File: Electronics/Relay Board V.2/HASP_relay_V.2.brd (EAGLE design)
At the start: 66.7 x 47.2 mm, 23 parts

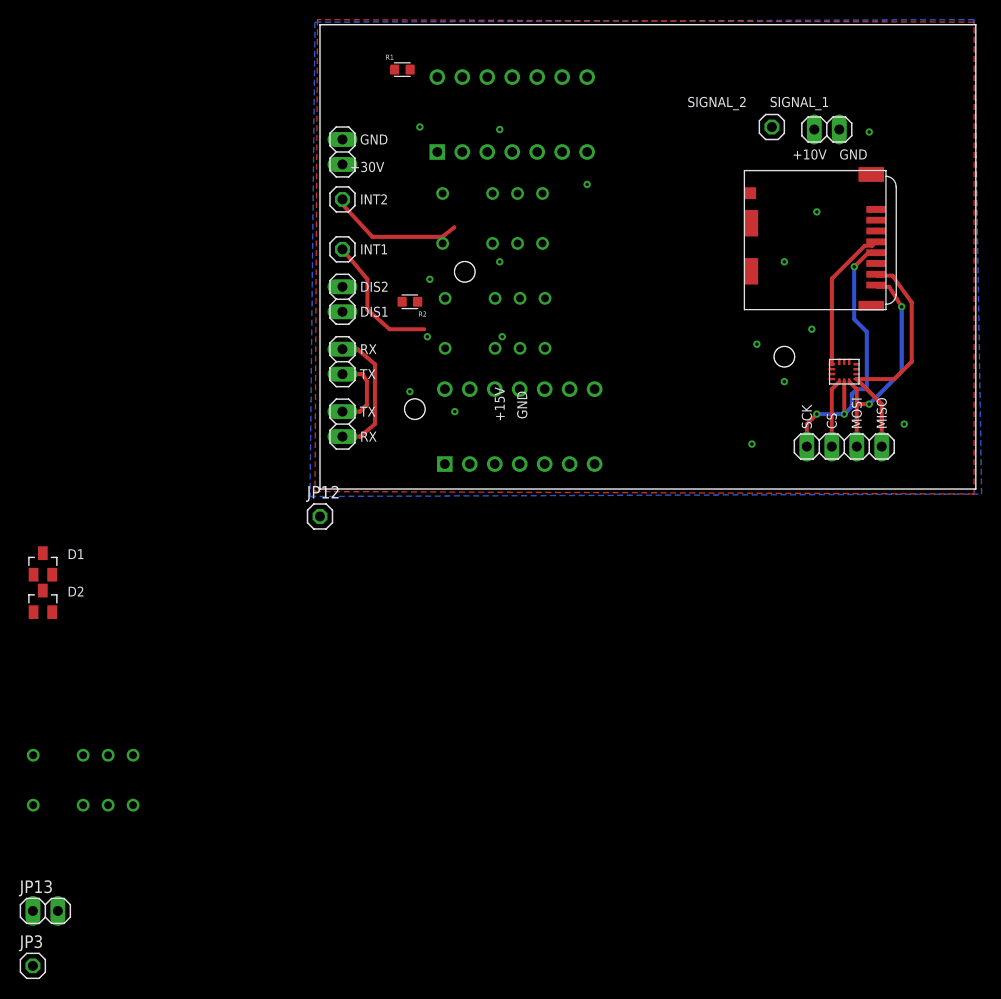
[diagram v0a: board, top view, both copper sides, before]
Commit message: got rid of unnecessary things on relay board, fixed the SD card routing, set up rough pass of board size
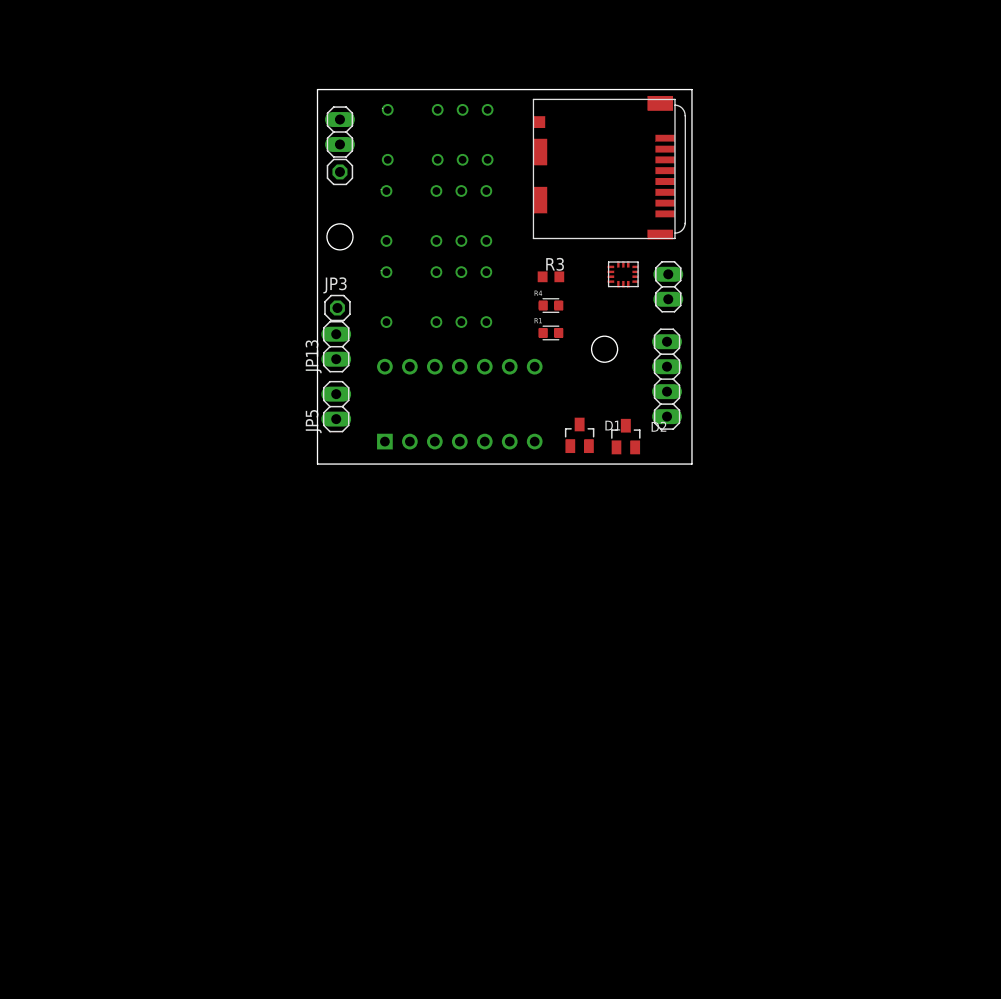
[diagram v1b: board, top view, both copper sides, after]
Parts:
- removed JP12, JP8, JP9: (no value), pinhead:1X01
- removed JP4, JP7: (no value), pinhead:1X02
- removed R2: 47k, CRGS0603J1K5:RESC1608X50N
- removed U$6: CD4093BE, NAND Gates:CD4093BE
- added R3: 1M, resistor:R0603
- added R4: 47k, CRGS0603J1K5:RESC1608X50N
- moved JP3 73.8 mm to (2.03, 15.9)
- moved JP13 64.6 mm to (1.91, 11.9), turned to 90 degrees
- moved D2 61.6 mm to (31.4, 2.79)
- moved U$8 60.9 mm to (5.97, 13.3)
- moved D1 56.2 mm to (26.7, 2.92)
- moved JP10 44.2 mm to (2.29, 29.7)
- moved R1 30.8 mm to (23.7, 13.3)
- moved U$1 24.6 mm to (31.1, 19.3)
- moved JP2 22.7 mm to (35.7, 18.0), turned to 270 degrees
- moved U$4 22.7 mm to (22.0, 33.1)
- moved U$2 20.0 mm to (6.10, 29.8)
- moved JP6 19.3 mm to (35.6, 8.64), turned to 270 degrees
- moved U$5 6.51 mm to (14.5, 6.10)
- moved U$3 5.72 mm to (5.97, 21.6)
- moved JP5 4.62 mm to (1.91, 5.84)
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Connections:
- removed net DIS1: JP4.1
- removed net DIS2: JP4.2
- removed net N$6: U$2.5
- removed net RX: JP5.2, JP7.2
- removed net TX: JP5.1, JP7.1
- new net N$5: U$4.VSS
- net +3V3: now also R3.1, R4.1; no longer R2.2, U$6.P$14
- net COIL2: now also U$5.P$10; no longer U$6.P$3
- net CS: now also R3.2, U$4.CD
- net GND: now also U$4.CD1; no longer U$4.VSS, U$6.P$7
- net INT1: now also JP5.1; no longer JP8.1
- net INT2: now also JP5.2, R4.2, U$5.P$8, U$5.P$9; no longer JP9.1, R2.1, U$6.P$1, U$6.P$2
- net MOSI: now also U$4.CMD; no longer U$4.DAT1
- net OUT1: now also U$2.5
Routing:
- net SCK: track 29.7 -> 0.00 mm, vias 3 -> 0
- net MISO: track 25.4 -> 0.00 mm
- net MOSI: track 23.7 -> 0.00 mm, vias 2 -> 0
- net +3V3: track 14.8 -> 0.00 mm
- net RX: track 13.7 -> 0.00 mm
- net INT2: track 13.7 -> 0.00 mm
- net INT1: track 13.6 -> 0.00 mm
- net TX: track 8.05 -> 0.00 mm
- net CS: track 6.93 -> 0.00 mm
- net GND: track 1.39 -> 0.00 mm, vias 16 -> 0
- removed copper zone on layer 1, net GND
- removed copper zone on layer 16, net GND
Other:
- board size 66.7 x 47.2 mm -> 38.1 x 38.1 mm
- board text removed: "+10V"
- board text removed: "+15V"
- board text removed: "+30V"
- board text removed: "7.2018"
- board text removed: "CS"
- board text removed: "DIS1"
- board text removed: "DIS2"
- board text removed: "GND"
- board text removed: "HASP Relay Board"
- board text removed: "INT1"
- board text removed: "INT2"
- board text removed: "MISO"
- board text removed: "MOSI"
- board text removed: "RX"
- board text removed: "SCK"
- board text removed: "SIGNAL_1"
- board text removed: "SIGNAL_2"
- board text removed: "TX"
- board text removed: "V. 2"

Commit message: Add files via upload
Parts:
- moved D1 24.6 mm to (8.89, 19.9), turned to 180 degrees
- moved D2 21.4 mm to (18.7, 20.1)
- moved U$8 2.79 mm to (5.97, 10.5)
- moved U$1 1.27 mm to (29.8, 19.3)
- moved U$3 0.76 mm to (5.97, 22.4)
- moved U$5 0.76 mm to (14.5, 5.33)
- moved R3 0.51 mm to (23.7, 19.6)
- moved U$2 0.25 mm to (6.10, 30.1)
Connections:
- removed net VDDIO: U$1.5
- net +3V3: now also U$1.5; no longer R1.2, R4.1, U$2.4, U$5.P$14
- net +5V: now also R1.2, R4.1, U$2.4, U$5.P$14
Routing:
- net +5V: track 0.00 -> 65.3 mm, vias 0 -> 1
- net MOSI: track 0.00 -> 48.3 mm, vias 0 -> 2
- net CS: track 0.00 -> 43.5 mm, vias 0 -> 3
- net SCK: track 0.00 -> 39.7 mm, vias 0 -> 2
- net COIL1: track 0.00 -> 39.1 mm, vias 0 -> 2
- net +3V3: track 0.00 -> 38.4 mm, vias 0 -> 2
- net INT2: track 0.00 -> 34.4 mm
- net DASIN: track 0.00 -> 29.3 mm
- net COIL2: track 0.00 -> 25.3 mm
- net DASOUT: track 0.00 -> 24.0 mm
- net OUT1: track 0.00 -> 20.4 mm
- net MISO: track 0.00 -> 19.6 mm, vias 0 -> 2
- net N$3: track 0.00 -> 14.4 mm
- net INT1: track 0.00 -> 11.0 mm
- net GND: track 0.00 -> 10.5 mm, vias 0 -> 2
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- added copper zone on layer 1, net GND
- added copper zone on layer 16, net GND
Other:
- board text added: "3V3"
- board text added: "5V"
- board text added: "7.2018"
- board text added: "ARDIN"
- board text added: "CS"
- board text added: "DASIN"
- board text added: "DASOUT"
- board text added: "GND"
- board text added: "HASP Relay Board"
- board text added: "INT1"
- board text added: "INT2"
- board text added: "MISO"
- board text added: "MOSI"
- board text added: "OUT1"
- board text added: "RELAY 1"
- board text added: "RELAY 2"
- board text added: "RELAY 3"
- board text added: "SCK"
- board text added: "V. 2"
